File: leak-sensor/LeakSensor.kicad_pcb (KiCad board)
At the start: 2 copper layers, 17.8 x 27.9 mm, 10 parts, among them P1 Mezzanine-Header

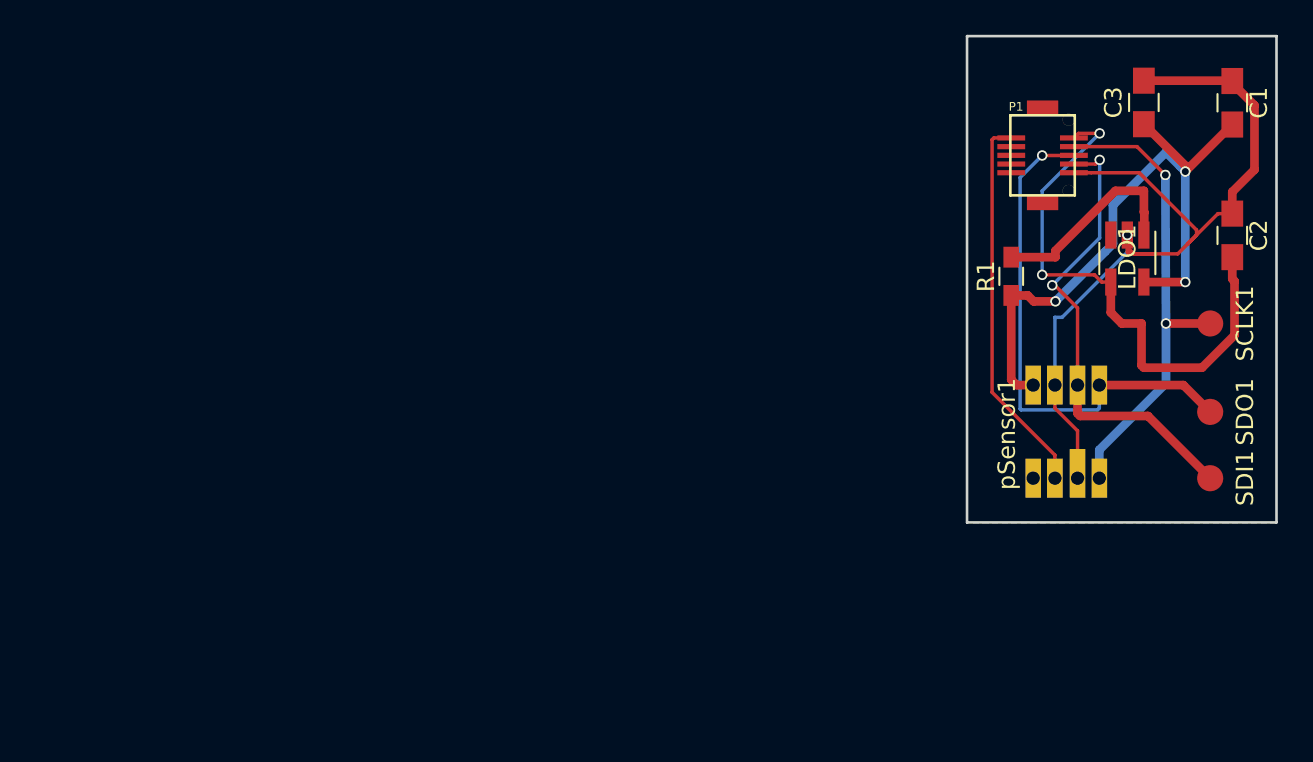
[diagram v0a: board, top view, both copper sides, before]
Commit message: Added changes from pneumatics project and leakSensor schematic
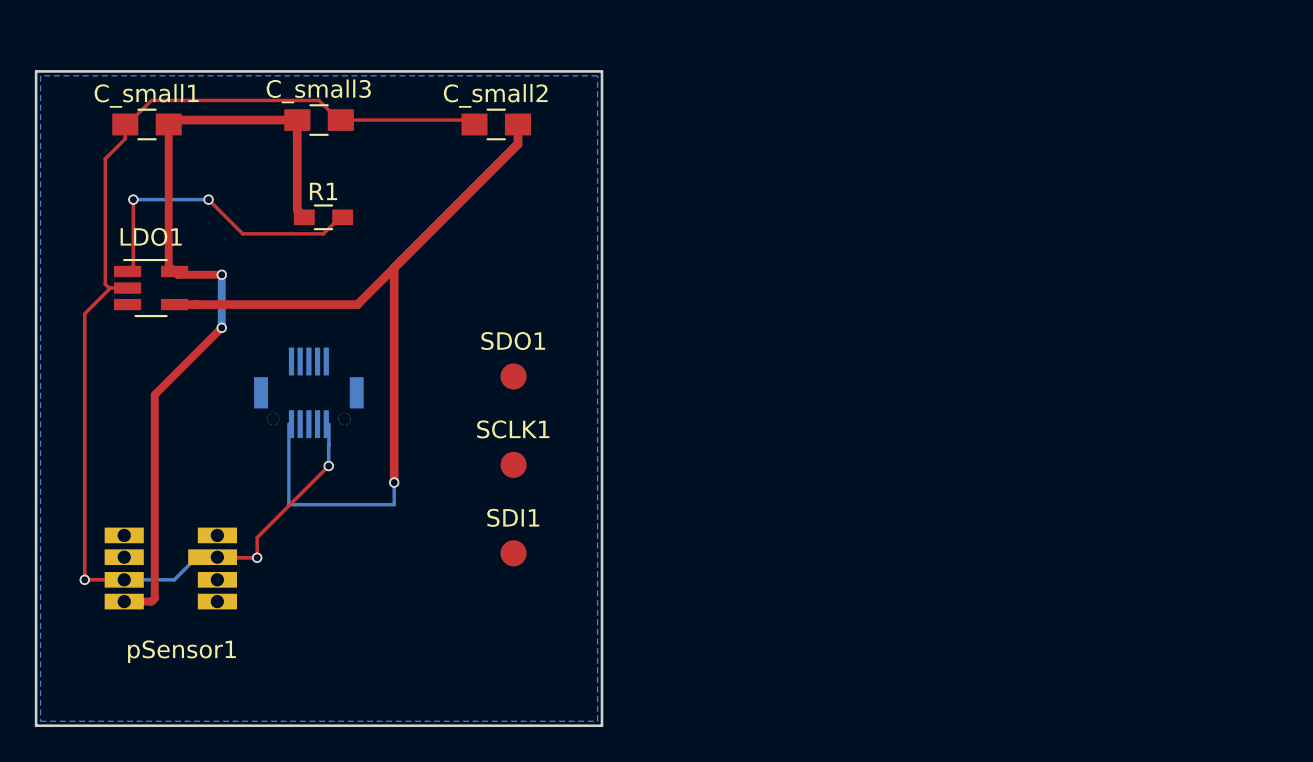
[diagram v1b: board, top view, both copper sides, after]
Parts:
- removed C1: 0.1uF, Capacitors_SMD:C_0805_HandSoldering
- removed C2: 0.47uF, Capacitors_SMD:C_0805_HandSoldering
- removed C3: 100nF, Capacitors_SMD:C_0805_HandSoldering
- added C_small1: 0.1uF, Capacitors_SMD:C_0805_HandSoldering, F.Cu at (90.7, 84.6)
- added C_small2: 0.47uF, Capacitors_SMD:C_0805_HandSoldering, F.Cu at (110.8, 84.6)
- added C_small3: 100nF, Capacitors_SMD:C_0805_HandSoldering, F.Cu at (100.6, 84.3)
- P1: moved to B.Cu
- moved LDO1 56.1 mm to (90.9, 94.0), turned to 0 degrees
- moved pSensor1 53.7 mm to (89.4, 112.0), turned to 0 degrees
- moved P1 44.3 mm to (100.0, 100.0), turned to 0 degrees
- moved SCLK1 40.8 mm to (111.8, 104.1), turned to 0 degrees
- moved SDI1 40.3 mm to (111.8, 109.2), turned to 0 degrees
- moved SDO1 40.1 mm to (111.8, 99.1), turned to 0 degrees
- moved R1 39.7 mm to (100.8, 89.9), turned to 0 degrees
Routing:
- net /SDO: track 29.9 -> 0.00 mm, vias 1 -> 0
- net /SCLK: track 27.5 -> 0.00 mm, vias 2 -> 0
- net /SDI: track 27.1 -> 0.00 mm, vias 2 -> 0
- net /VDD: track 32.5 -> 59.0 mm, vias 2 -> 1
- net /GND: track 50.3 -> 74.1 mm, vias 1 -> 3
- net /CSB: track 22.1 -> 0.00 mm
- net /Vreg: track 37.9 -> 46.6 mm, vias 3 -> 2
- net Net-(LDO1-Pad1): track 12.0 -> 17.5 mm, vias 0 -> 2
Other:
- board size 17.8 x 27.9 mm -> 32.5 x 37.6 mm
- net class Default: clearance 0.2 -> 0.1524
- rule trace_clearance: 0.2 -> 0.1524
- rule trace_min: 0.2 -> 0.1524
- rule via_min_drill: 0.3 -> 0.3302
